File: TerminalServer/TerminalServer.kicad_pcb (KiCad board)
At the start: 4 copper layers, 135 x 72 mm, 128 parts, among them J1 RJ45_LED, J10 Conn_01x10_Pin, J11 SI-60118-F, J12 Conn_01x08_Pin, J2 RJ45_LED, J3 RJ45_LED, J4 RJ45_LED, J5 RJ45_LED, J6 RJ45_LED, J7 USB_C_Receptacle_USB2.0_14P, J8 Barrel_Jack_Switch, J9 Conn_PIC_ICSP_ICD, SW1 SW_Push, SW2 SW_SPDT, U1 PIC32MX795F512L-80x-PT, U10 24LC16, U11 ENC28J60x-ML, U12 ESP32-S3-WROOM-1, U2 XR32330EBERTR-F, U3 XR32330EBERTR-F, U4 XR32330EBERTR-F, U5 XR32330EBERTR-F, U6 XR32330EBERTR-F, U7 XR32330EBERTR-F, U9 TPS82130, Y1 ASEMB-8.000MHZ-LC-T, Y2 ASEMB-25.000MHZ-LC-T

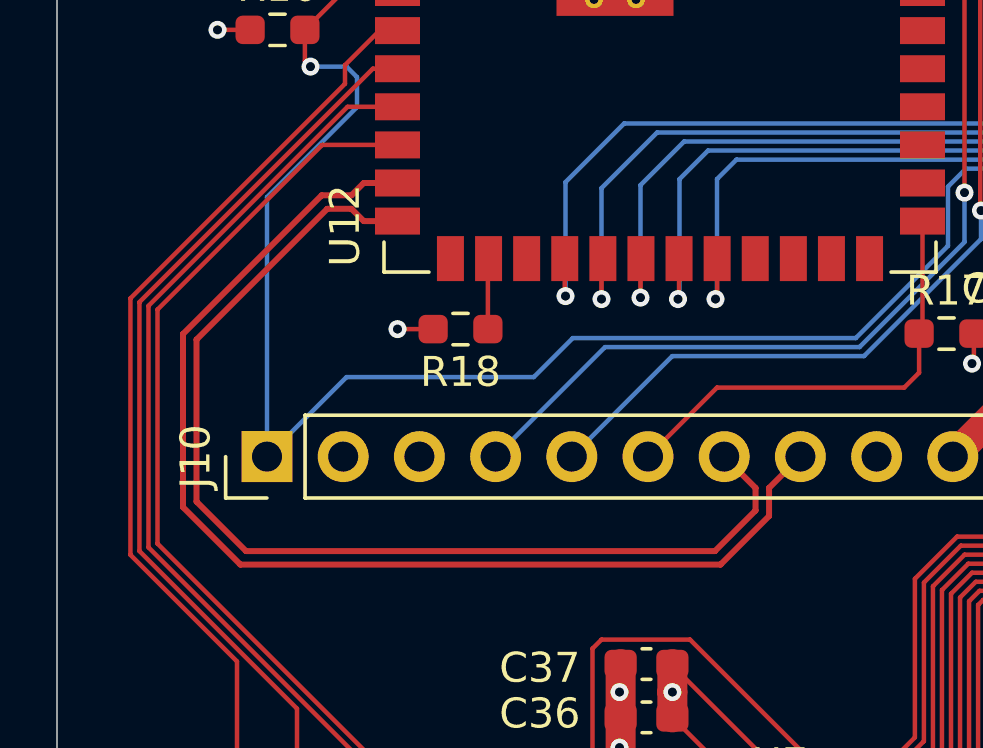
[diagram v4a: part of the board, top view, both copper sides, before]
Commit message: Improved render interface
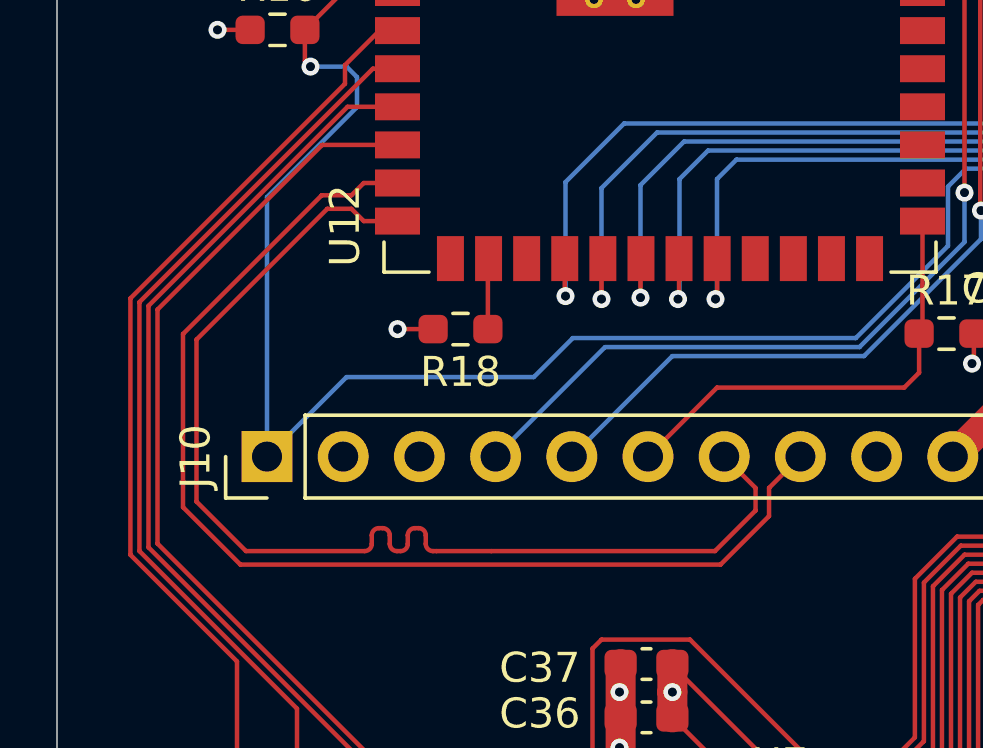
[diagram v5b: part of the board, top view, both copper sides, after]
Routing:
- net /ESP_USB_P: track 36.2 -> 38.3 mm
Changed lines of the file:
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@@
+	)
+	(segment
+		(start 81.224999 86.98)
+		(end 80.814999 87.39)
+		(width 0.15)
+		(layer "F.Cu")
+		(net 228)
+	)
+	(segment
+		(start 94.735001 98.083197)
+		(end 94.735001 97.144999)
+		(width 0.15)
+		(layer "F.Cu")
+		(net 228)
+	)
+	(segment
+		(start 75.2 97.786394)
+		(end 77.113606 99.7)
+		(width 0.15)
+		(layer "F.Cu")
+		(net 228)
+	)
+	(segment
+		(start 93.118198 99.7)
+		(end 94.735001 98.083197)
+		(width 0.15)
+		(layer "F.Cu")
+		(net 228)
+	)
+	(segment
+		(start 94.735001 97.144999)
+		(end 95.78 96.1)
+		(width 0.15)
+		(layer "F.Cu")
+		(net 228)
+	)
+	(segment
+		(start 79.823606 87.39)
+		(end 75.2 92.013606)
+		(width 0.15)
+		(layer "F.Cu")
+		(net 228)
 	)
 	(segment
 		(start 75.2 92.013606)
 		(end 75.2 97.786394)
-		(width 0.2)
+		(width 0.15)
 		(layer "F.Cu")
 		(net 228)
 	)
 	(segment
-		(start 94.735001 97.144999)
-		(end 95.78 96.1)
-		(width 0.2)
-		(layer "F.Cu")
-		(net 228)
-	)
-	(segment
-		(start 93.118198 99.7)
-		(end 94.735001 98.083197)
-		(width 0.2)
-		(layer "F.Cu")
-		(net 228)
-	)
-	(segment
-		(start 75.2 97.786394)
-		(end 77.113606 99.7)
-		(width 0.2)
+		(start 77.113606 99.7)
+		(end 93.118198 99.7)
+		(width 0.15)
 		(layer "F.Cu")
 		(net 228)
@@
 		(start 80.814999 87.39)
 		(end 79.823606 87.39)
-		(width 0.2)
-		(layer "F.Cu")
-		(net 228)
-	)
-	(segment
-		(start 79.823606 87.39)
-		(end 75.2 92.013606)
-		(width 0.2)
-		(layer "F.Cu")
-		(net 228)
-	)
-	(segment
-		(start 94.735001 98.083197)
-		(end 94.735001 97.144999)
-		(width 0.2)
-		(layer "F.Cu")
-		(net 228)
-	)
-	(segment
-		(start 81.224999 86.98)
-		(end 80.814999 87.39)
-		(width 0.2)
-		(layer "F.Cu")
-		(net 228)
-	)
-	(segment
-		(start 77.113606 99.7)
-		(end 93.118198 99.7)
-		(width 0.2)
+		(width 0.15)
 		(layer "F.Cu")
 		(net 228)
@@
 		(start 82.35 86.98)
 		(end 81.224999 86.98)
-		(width 0.2)
+		(width 0.15)
 		(layer "F.Cu")
 		(net 228)
+	)
+	(segment
+		(start 82.35 88.25)
+		(end 81.224999 88.25)
+		(width 0.15)
+		(layer "F.Cu")
+		(net 229)
+	)
+	(segment
+		(start 83.531993 99.25)
+		(end 83.651993 99.25)
+		(width 0.15)
+		(layer "F.Cu")
+		(net 229)
+	)
+	(segment
+		(start 82.691993 99.01)
+		(end 82.691993 98.724791)
+		(width 0.15)
+		(layer "F.Cu")
+		(net 229)
+	)
+	(segment
+		(start 83.291993 98.724791)
+		(end 83.291993 99.01)
+		(width 0.15)
+		(layer "F.Cu")
+		(net 229)
+	)
+	(segment
+		(start 83.651993 99.25)
+		(end 85.480063 99.25)
+		(width 0.15)
+		(layer "F.Cu")
+		(net 229)
+	)
+	(segment
+		(start 94.284999 97.144999)
+		(end 93.24 96.1)
+		(width 0.15)
+		(layer "F.Cu")
+		(net 229)
+	)
+	(segment
+		(start 75.65 97.6)
+		(end 77.3 99.25)
+		(width 0.15)
+		(layer "F.Cu")
+		(net 229)
+	)
+	(segment
+		(start 81.491993 99.01)
+		(end 81.491993 98.724815)
+		(width 0.15)
+		(layer "F.Cu")
+		(net 229)
+	)
+	(segment
+		(start 81.731993 98.484815)
+		(end 81.851993 98.484815)
+		(width 0.15)
+		(layer "F.Cu")
+		(net 229)
+	)
+	(segment
+		(start 85.480063 99.25)
+		(end 92.931802 99.25)
+		(width 0.15)
+		(layer "F.Cu")
+		(net 229)
+	)
+	(segment
+		(start 82.331993 99.25)
+		(end 82.451993 99.25)
+		(width 0.15)
+		(layer "F.Cu")
+		(net 229)
+	)
+	(segment
+		(start 82.091993 98.724815)
+		(end 82.091993 99.01)
+		(width 0.15)
+		(layer "F.Cu")
+		(net 229)
+	)
+	(segment
+		(start 75.65 92.2)
+		(end 75.65 97.6)
+		(width 0.15)
+		(layer "F.Cu")
+		(net 229)
+	)
+	(segment
+		(start 80.01 87.84)
+		(end 75.65 92.2)
+		(width 0.15)
+		(layer "F.Cu")
+		(net 229)
+	)
+	(segment
+		(start 82.931993 98.484791)
+		(end 83.051993 98.484791)
+		(width 0.15)
+		(layer "F.Cu")
+		(net 229)
 	)
 	(segment
 		(start 80.814999 87.84)
 		(end 80.01 87.84)
-		(width 0.2)
-		(layer "F.Cu")
-		(net 229)
-	)
-	(segment
-		(start 80.01 87.84)
-		(end 75.65 92.2)
-		(width 0.2)
-		(layer "F.Cu")
-		(net 229)
-	)
-	(segment
-		(start 75.65 92.2)
-		(end 75.65 97.6)
-		(width 0.2)
+		(width 0.15)
 		(layer "F.Cu")
 		(net 229)
@@
 		(start 94.284999 97.896803)
 		(end 94.284999 97.144999)
-		(width 0.2)
-		(layer "F.Cu")
-		(net 229)
-	)
-	(segment
-		(start 94.284999 97.144999)
-		(end 93.24 96.1)
-		(width 0.2)
+		(width 0.15)
+		(layer "F.Cu")
+		(net 229)
+	)
+	(segment
+		(start 77.3 99.25)
+		(end 81.251993 99.25)
+		(width 0.15)
+		(layer "F.Cu")
+		(net 229)
+	)
+	(segment
+		(start 81.224999 88.25)
+		(end 80.814999 87.84)
+		(width 0.15)
 		(layer "F.Cu")
 		(net 229)
@@
 		(start 92.931802 99.25)
 		(end 94.284999 97.896803)
-		(width 0.2)
-		(layer "F.Cu")
-		(net 229)
-	)
-	(segment
-		(start 81.224999 88.25)
-		(end 80.814999 87.84)
-		(width 0.2)
-		(layer "F.Cu")
-		(net 229)
-	)
-	(segment
-		(start 82.35 88.25)
-		(end 81.224999 88.25)
-		(width 0.2)
-		(layer "F.Cu")
-		(net 229)
-	)
-	(segment
-		(start 77.3 99.25)
-		(end 92.931802 99.25)
-		(width 0.2)
-		(layer "F.Cu")
-		(net 229)
-	)
-	(segment
-		(start 75.65 97.6)
-		(end 77.3 99.25)
-		(width 0.2)
+		(width 0.15)
+		(layer "F.Cu")
+		(net 229)
+	)
+	(arc
+		(start 81.851993 98.484815)
+		(mid 82.021699 98.555109)
+		(end 82.091993 98.724815)
+		(width 0.15)
+		(layer "F.Cu")
+		(net 229)
+	)
+	(arc
+		(start 81.491993 98.724815)
+		(mid 81.562287 98.555109)
+		(end 81.731993 98.484815)
+		(width 0.15)
+		(layer "F.Cu")
+		(net 229)
+	)
+	(arc
+		(start 83.051993 98.484791)
+		(mid 83.221699 98.555085)
+		(end 83.291993 98.724791)
+		(width 0.15)
+		(layer "F.Cu")
+		(net 229)
+	)
+	(arc
+		(start 83.291993 99.01)
+		(mid 83.362287 99.179706)
+		(end 83.531993 99.25)
+		(width 0.15)
+		(layer "F.Cu")
+		(net 229)
+	)
+	(arc
+		(start 82.091993 99.01)
+		(mid 82.162287 99.179706)
+		(end 82.331993 99.25)
+		(width 0.15)
+		(layer "F.Cu")
+		(net 229)
+	)
+	(arc
+		(start 81.251993 99.25)
+		(mid 81.421699 99.179706)
+		(end 81.491993 99.01)
+		(width 0.15)
+		(layer "F.Cu")
+		(net 229)
+	)
+	(arc
+		(start 82.691993 98.724791)
+		(mid 82.762287 98.555085)
+		(end 82.931993 98.484791)
+		(width 0.15)
+		(layer "F.Cu")
+		(net 229)
+	)
+	(arc
+		(start 82.451993 99.25)
+		(mid 82.621699 99.179706)
+		(end 82.691993 99.01)
+		(width 0.15)
 		(layer "F.Cu")
 		(net 229)
@@
 		)
 	)
+	(generated
+		(type tuning_pattern)
+		(name "Tuning Pattern")
+		(layer "F.Cu")
+		(base_line
+			(pts
+				(xy 81.251993 99.25) (xy 85.480063 99.25)
+			)
+		)
+		(base_line_coupled
+			(pts
+				(xy 81.251993 99.7) (xy 81.28941 99.7)
+			)
+		)
+		(corner_radius_percent 80)
+		(end
+			(xy 85.480063 99.25)
+		)
+		(initial_side "left")
+		(last_diff_pair_gap 0.18)
+		(last_netname "/ESP_USB_P")
+		(last_status "tuned")
+		(last_track_width 0.15)
+		(last_tuning "0.0000 mm (tuned)")
+		(max_amplitude 1)
+		(min_amplitude 0.2)
+		(min_spacing 0.6)
+		(origin
+			(xy 81.251993 99.25)
+		)
+		(override_custom_rules no)
+		(rounded yes)
+		(single_sided no)
+		(target_length 1000000)
+		(target_length_max 1000000)
+		(target_length_min 0)
+		(target_skew 0)
+		(target_skew_max 0.1)
+		(target_skew_min -0.1)
+		(tuning_mode "diff_pair_skew")
+		(members "00726cf1-4e94-468e-b038-e9f6462e923b" "0a35b19d-c99d-4726-af86-8278924fb1ce"
+			"26536fbd-bc1c-4081-b1aa-8f6d29831651" "490ff514-dd04-46da-bd2e-c07d11180ee6"
+			"49c2dc1f-92d8-4730-9191-e71050451fe4" "56656d40-88fa-4fa5-b9e4-7d0713a8220f"
+			"5c8e2096-9dbc-43d9-8ae4-8fa33614ea2c" "70c177ac-6d5d-4478-98f5-e85f421df64f"
+			"743c96d7-eece-44d6-b31e-f4b37de354a1" "75176927-01b6-4694-9371-f943059d4078"
+			"77f3228e-d21d-41d1-bdca-bf45236c00e6" "84b05f2e-bbd2-4aca-aba8-d631efa5ced2"
+			"84c8d27b-d52c-4f37-ab6e-32b3ffa6c30c" "b92d13fa-9a3e-4541-b59e-99870d058324"
+			"c752b7d3-d0d2-4c93-adf4-19de7b44b6c6" "e10fd845-ca3f-4503-ac41-556b878a6d03"
+			"f4cc9c2b-9eaf-4716-997b-e691adaae377"
+		)
+	)

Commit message: Almost complete
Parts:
- D1, D2, D3: value 1N5819WS -> V8PAN50-M3/I; footprint Diode_SMD:D_SOD-323 -> Diode_SMD:Vishay_SMPA
- moved D1 0.50 mm to (182.5, 77.0)
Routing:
- net /SWIN: track 17.1 -> 14.2 mm
- net /USB_VBUS: track 59.0 -> 57.7 mm
- net VCC: track 38.3 -> 37.7 mm
- net Net-(D3-A): track 111.8 -> 111.2 mm
- net Net-(D2-A): track 16.8 -> 16.2 mm

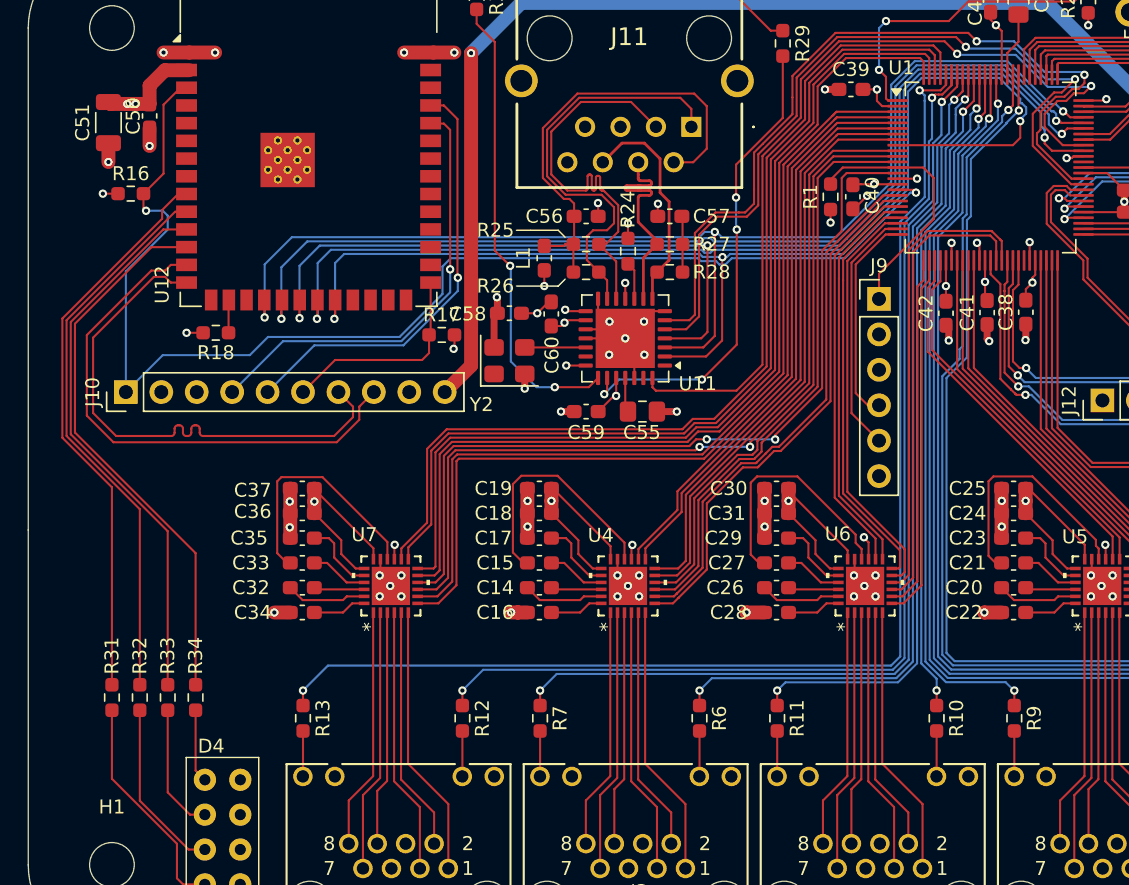
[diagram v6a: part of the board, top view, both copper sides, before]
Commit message: Added SD card
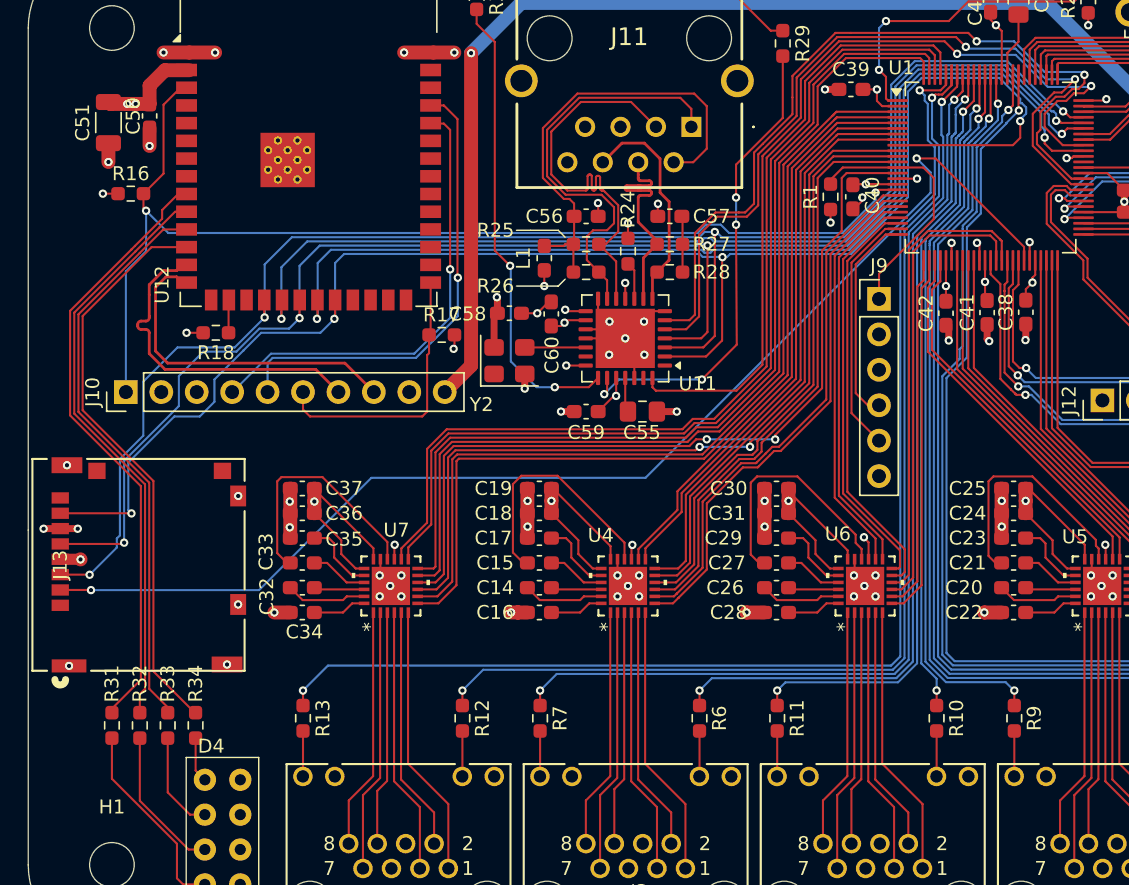
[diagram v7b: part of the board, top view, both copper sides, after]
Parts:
- added J13: Micro_SD_Card, MolexSD:503182-1852_MOL, F.Cu at (67.7, 108.5)
- moved R31 2.00 mm to (77.0, 120.0)
- moved R32 2.00 mm to (79.0, 120.0)
- moved R33 2.00 mm to (81.0, 120.0)
- moved R34 2.00 mm to (83.0, 120.0)
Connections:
- J10 pad 7: /ESP_USB_P -> /ESP_USB_N
- J10 pad 8: /ESP_USB_N -> /ESP_USB_P
- U1 pad 44: unconnected-(U1-RB15-Pad44) -> /SD_CS
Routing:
- net /SD_CS: track 0.00 -> 88.4 mm, vias 0 -> 2
- net /SPI_MISO: track 87.8 -> 116.9 mm, vias 3 -> 4
- net /SPI_SCK: track 83.2 -> 112.1 mm, vias 3 -> 4
- net /SPI_MOSI: track 87.3 -> 115.8 mm, vias 3 -> 4
- net /ESP_USB_N: track 38.4 -> 24.1 mm
- net /ESP_USB_P: track 38.3 -> 24.1 mm
- net /ESP_EN: track 91.5 -> 80.7 mm
- net /ESP_IO0: track 15.3 -> 19.9 mm
- net /LED1: track 40.7 -> 44.0 mm
- net /ESP_TX: track 31.1 -> 33.7 mm
- net GND: track 119.2 -> 121.4 mm, vias 102 -> 109
- net VDD: track 158.2 -> 160.3 mm, vias 41 -> 42
- net Net-(D4-LED_A3): track 9.21 -> 7.21 mm
- net Net-(D4-LED_A4): track 5.26 -> 3.26 mm
- net Net-(D4-LED_A2): track 12.6 -> 10.6 mm
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
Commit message: Final cleanup
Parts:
- removed R34: 100R, Resistor_SMD:R_0603_1608Metric_Pad0.98x0.95mm_HandSolder
- D4: value XL-DZ234SYGD-4 -> 564-0100-132F; footprint XINGLIGHT:XL-DZ234SYGD-4 -> Triple LED:5640100222F
- J13: value Micro_SD_Card -> 503398-1892; footprint MolexSD:503182-1852_MOL -> KiCad:5033981892
- J7: value USB_C_Receptacle_USB2.0_14P -> USB_B; footprint Connector_USB:USB_C_Receptacle_GCT_USB4105-xx-A_16P_TopMnt_Horizontal -> Connector_USB:USB_B_OST_USB-B1HSxx_Horizontal
- moved J7 8.91 mm to (176.8, 74.8), turned to 90 degrees
- moved J13 8.40 mm to (72.2, 115.6)
- moved D3 4.00 mm to (182.5, 88.0)
- moved D2 3.50 mm to (182.5, 84.0)
- moved D1 3.00 mm to (182.5, 80.0)
- moved J8 2.80 mm to (164.6, 73.3)
- moved D4 2.73 mm to (86.5, 131.5)
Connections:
- J13 pad 14: (no net) -> GND
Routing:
- net /LED4: track 41.3 -> 0.00 mm
- net /USB_VBUS: track 57.7 -> 47.0 mm, vias 2 -> 1
- net Net-(D2-A): track 16.2 -> 20.3 mm
- net Net-(D4-LED_A4): track 3.26 -> 0.00 mm
- net GND: track 121.4 -> 118.7 mm, vias 109 -> 108
- net Net-(D3-A): track 111.2 -> 112.5 mm
- net /SWIN: track 14.2 -> 12.9 mm
- net VCC: track 37.7 -> 36.8 mm
- net Net-(D4-A_POSITION_1): track 7.21 -> 7.99 mm
- net /USBD_P: track 50.9 -> 50.2 mm, vias 3 -> 1
- net /U2DTR: track 54.9 -> 54.2 mm
- net /U2DSR: track 52.7 -> 51.9 mm
- net /U2CTS: track 51.9 -> 51.2 mm
- net /U2STATUS: track 50.5 -> 49.8 mm
- net Net-(D4-A_POSITION_3): track 14.2 -> 13.5 mm
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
